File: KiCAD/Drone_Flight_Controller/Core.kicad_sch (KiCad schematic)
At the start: 24 parts, among them SW1 SW_Push, SW2 SW_Push, U5 BNO055, U6 ESP32-S3-MINI-1, U7 DPS368, U8 TLV75533PDBV

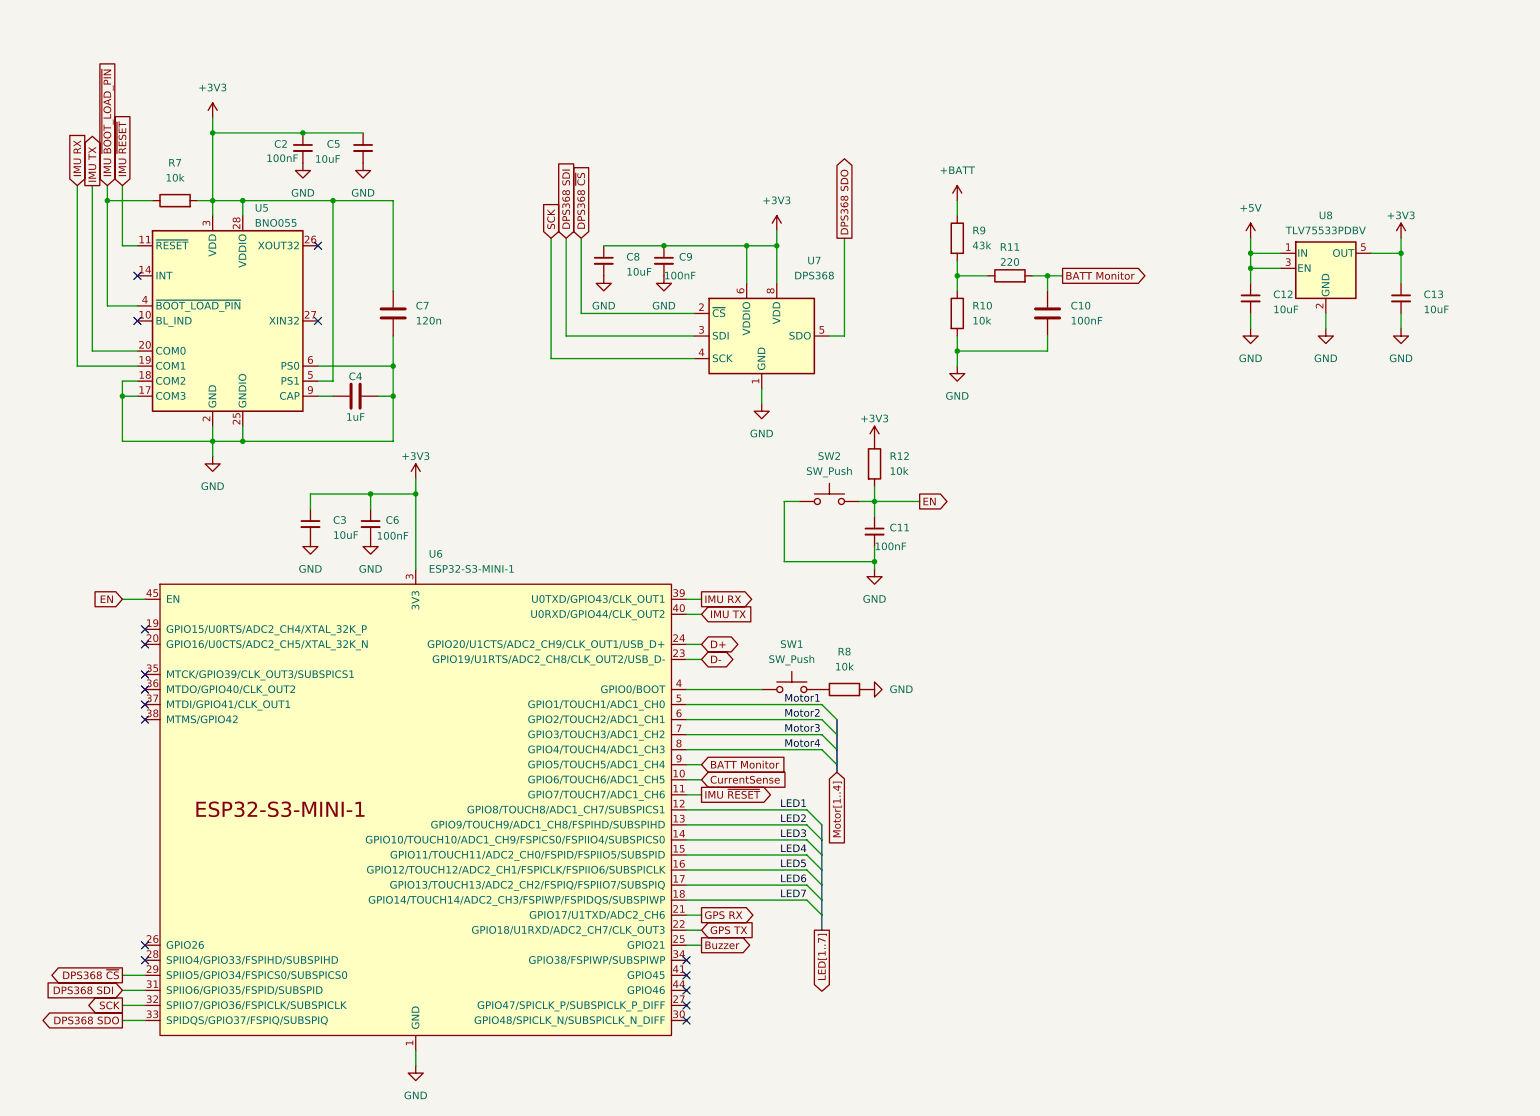
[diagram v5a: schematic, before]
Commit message: Add µSD Card Holder
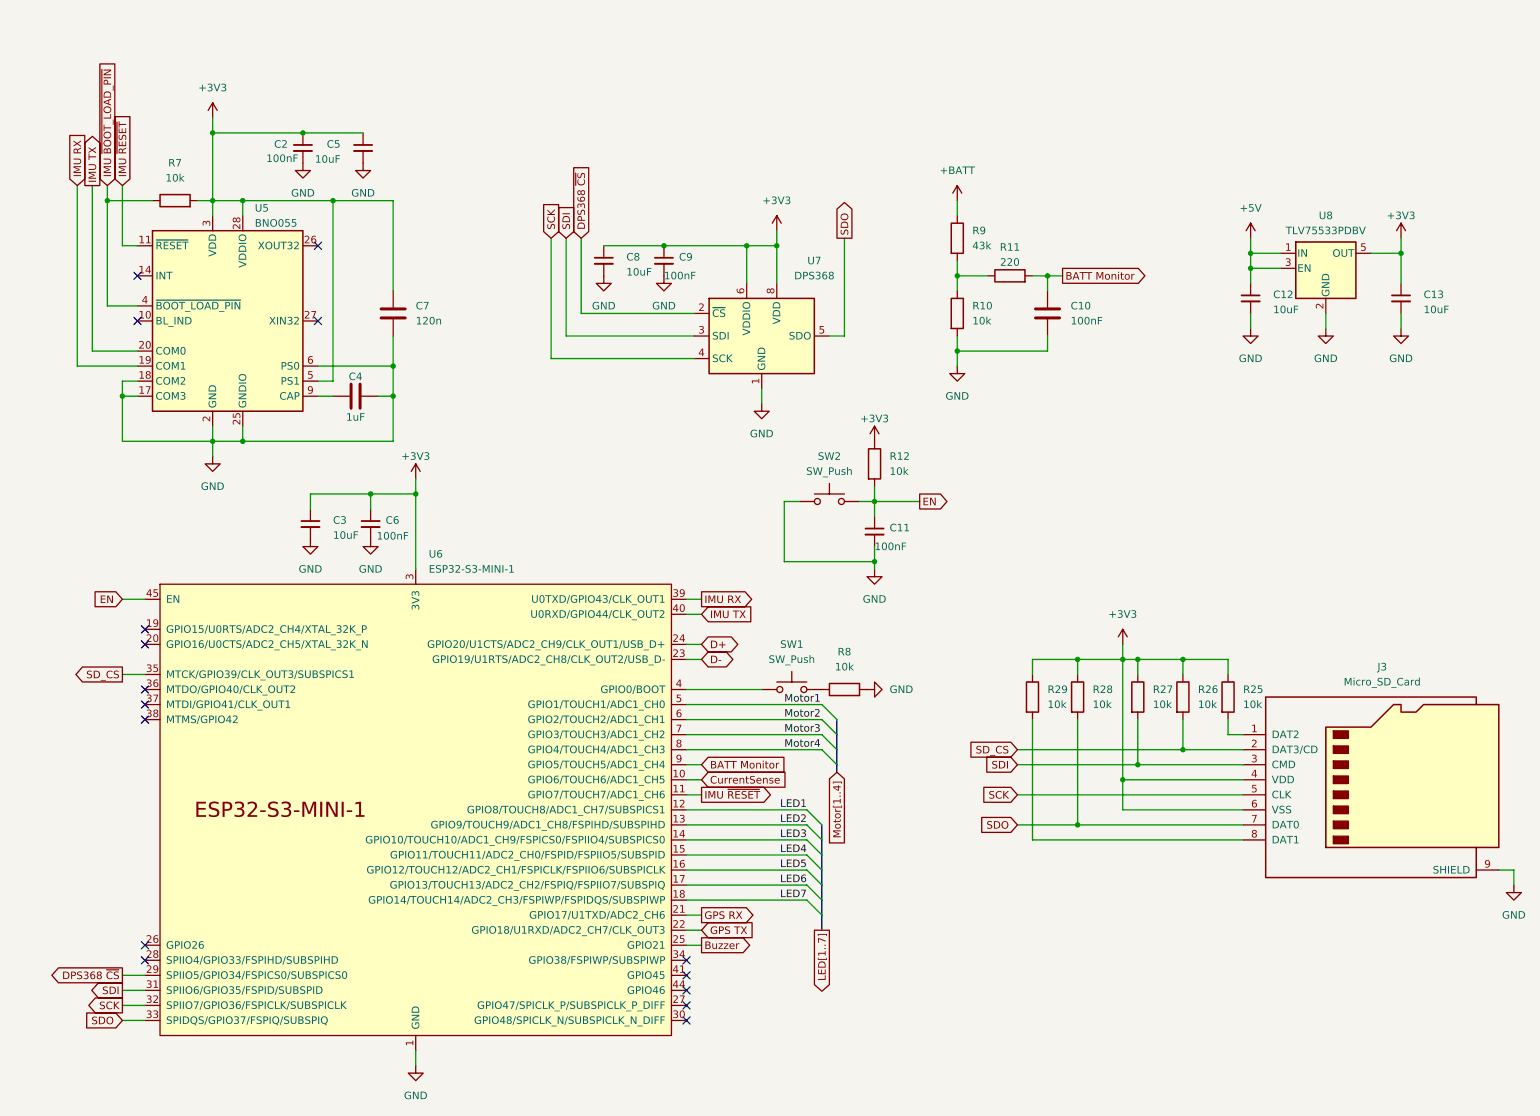
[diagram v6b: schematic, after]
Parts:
- added J3: Micro_SD_Card, Connector_Card:microSD_HC_Hirose_DM3D-SF, symbol Connector:Micro_SD_Card
- added R25, R26, R27, R28, R29: 10k, Resistor_SMD:R_0805_2012Metric_Pad1.20x1.40mm_HandSolder, symbol Device:R
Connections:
- net +3V3: now also J3.4 (VDD), J3.6 (VSS), R25.1, R26.1, R27.1, R28.1, R29.1
- net GND: now also J3.9 (SHIELD)
- net SCK: now also J3.5 (CLK)
- net SD_CS: now reaches U6.35 (MTCK/GPIO39/CLK_OUT3/SUBSPICS1)
- net SD_CS: now also J3.2 (DAT3/CD), R26.2
- net DPS368 SDI renamed SDI
- net SDI: now also J3.3 (CMD), R27.2
- net DPS368 SDO renamed SDO
- net SDO: now also J3.7 (DAT0), R28.2
- new net: J3.1 (DAT2), R25.2
- new net: J3.8 (DAT1), R29.2
- no-connect marks 17 -> 16

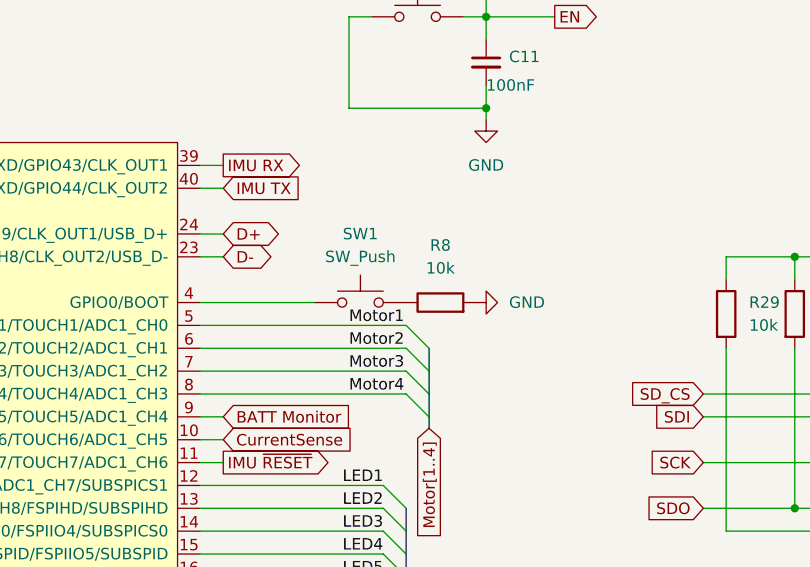
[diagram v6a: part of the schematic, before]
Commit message: Add debouncing C to button
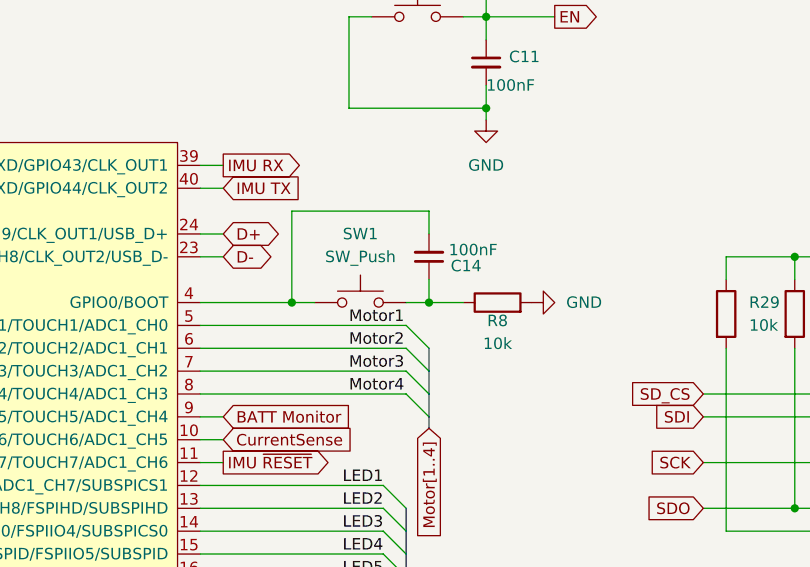
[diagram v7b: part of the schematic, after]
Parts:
- added C14: 100nF, Capacitor_SMD:C_0805_2012Metric, symbol Device:C_Small
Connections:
- net at SW1.1, U6.4 (GPIO0/BOOT): now also C14.2
- net at R8.1, SW1.2: now also C14.1
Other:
- moved on the sheet: R8
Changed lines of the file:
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@@
 	)
 	(junction
+		(at 158.75 123.19)
+		(diameter 0)
+		(color 0 0 0 0)
+	)
+	(junction
 		(at 209.55 135.89)
 		(diameter 0)
@@
 	)
 	(junction
+		(at 143.51 123.19)
+		(diameter 0)
+		(color 0 0 0 0)
+	)
+	(junction
 		(at 254 49.53)
 		(diameter 0)
@@
 	(wire
 		(pts
+			(xy 158.75 113.03) (xy 143.51 113.03)
+		)
+		(stroke
+			(width 0)
+			(type default)
+		)
+	)
+	(wire
+		(pts
 			(xy 87.63 87.63) (xy 87.63 90.17)
 		)
@@
 	(wire
 		(pts
+			(xy 143.51 113.03) (xy 143.51 123.19)
+		)
+		(stroke
+			(width 0)
+			(type default)
+		)
+	)
+	(wire
+		(pts
 			(xy 254 49.53) (xy 254 46.99)
 		)
@@
 	(wire
 		(pts
+			(xy 162.56 123.19) (xy 158.75 123.19)
+		)
+		(stroke
+			(width 0)
+			(type default)
+		)
+	)
+	(wire
+		(pts
 			(xy 50.8 40.64) (xy 53.34 40.64)
 		)
@@
 	(wire
 		(pts
+			(xy 158.75 120.65) (xy 158.75 123.19)
+		)
+		(stroke
+			(width 0)
+			(type default)
+		)
+	)
+	(wire
+		(pts
 			(xy 83.82 63.5) (xy 83.82 68.58)
 		)
@@
 	(wire
 		(pts
-			(xy 133.35 123.19) (xy 146.05 123.19)
+			(xy 133.35 123.19) (xy 143.51 123.19)
 		)
 		(stroke
@@
 	(wire
 		(pts
+			(xy 158.75 115.57) (xy 158.75 113.03)
+		)
+		(stroke
+			(width 0)
+			(type default)
+		)
+	)
+	(wire
+		(pts
 			(xy 179.07 68.58) (xy 179.07 66.04)
 		)
@@
 	(wire
 		(pts
+			(xy 143.51 123.19) (xy 146.05 123.19)
+		)
+		(stroke
+			(width 0)
+			(type default)
+		)
+	)
+	(wire
+		(pts
 			(xy 162.56 91.44) (xy 165.1 91.44)
 		)
@@
 	(wire
 		(pts
+			(xy 158.75 123.19) (xy 156.21 123.19)
+		)
+		(stroke
+			(width 0)
+			(type default)
+		)
+	)
+	(wire
+		(pts
 			(xy 115.57 59.69) (xy 134.62 59.69)
 		)
@@
 	(symbol
 		(lib_id "power:GND")
-		(at 163.83 123.19 90)
+		(at 170.18 123.19 90)
 		(unit 1)
 		(exclude_from_sim no)
@@
 		(fields_autoplaced yes)
 		(property "Reference" "#PWR049"
-			(at 170.18 123.19 0)
+			(at 176.53 123.19 0)
 			(effects
 				(font
@@
 		)
 		(property "Value" "GND"
-			(at 167.64 123.1899 90)
+			(at 173.99 123.1899 90)
 			(effects
 				(font
@@
 		)
 		(property "Footprint" ""
-			(at 163.83 123.19 0)
+			(at 170.18 123.19 0)
 			(effects
 				(font
@@
 		)
 		(property "Datasheet" ""
-			(at 163.83 123.19 0)
+			(at 170.18 123.19 0)
 			(effects
 				(font
@@
 		)
 		(property "Description" "Power symbol creates a global label with name \"GND\" , ground"
-			(at 163.83 123.19 0)
+			(at 170.18 123.19 0)
 			(effects
 				(font
@@
 	(symbol
 		(lib_id "Device:C_Small")
+		(at 158.75 118.11 180)
+		(unit 1)
+		(exclude_from_sim no)
+		(in_bom yes)
+		(on_board yes)
+		(dnp no)
+		(property "Reference" "C14"
+			(at 164.592 119.126 0)
+			(effects
+				(font
+					(size 1.27 1.27)
+				)
+				(justify left)
+			)
+		)
+		(property "Value" "100nF"
+			(at 166.37 117.348 0)
+			(effects
+				(font
+					(size 1.27 1.27)
+				)
+				(justify left)
+			)
+		)
+		(property "Footprint" "Capacitor_SMD:C_0805_2012Metric"
+			(at 158.75 118.11 0)
+			(effects
+				(font
+					(size 1.27 1.27)
+				)
+				(hide yes)
+			)
+		)
+		(property "Datasheet" "~"
+			(at 158.75 118.11 0)
+			(effects
+				(font
+					(size 1.27 1.27)
+				)
+				(hide yes)
+			)
+		)
+		(property "Description" "Unpolarized capacitor, small symbol"
+			(at 158.75 118.11 0)
+			(effects
+				(font
+					(size 1.27 1.27)
+				)
+				(hide yes)
+			)
+		)
+		(pin "1"
+		)
+		(pin "2"
+		)
+		(instances
+			(project "Drone_Flight_Controller"
+				(path "/51ab9491-7068-4b24-bb38-47a0c739796e/c31581c9-6b89-48da-8db2-6196211c3da7"
+					(reference "C14")
+					(unit 1)
+				)
+			)
+		)
+	)
+	(symbol
+		(lib_id "Device:C_Small")
 		(at 80.01 95.25 0)
 		(unit 1)
@@
 	(symbol
 		(lib_id "Device:R")
-		(at 160.02 123.19 90)
+		(at 166.37 123.19 90)
 		(unit 1)
 		(exclude_from_sim no)
@@
 		(on_board yes)
 		(dnp no)
-		(fields_autoplaced yes)
 		(property "Reference" "R8"
-			(at 160.02 116.84 90)
+			(at 166.37 125.222 90)
 			(effects
 				(font
@@
 		)
 		(property "Value" "10k"
-			(at 160.02 119.38 90)
+			(at 166.37 127.762 90)
 			(effects
 				(font
@@
 		)
 		(property "Footprint" "Resistor_SMD:R_0805_2012Metric_Pad1.20x1.40mm_HandSolder"
-			(at 160.02 124.968 90)
+			(at 166.37 124.968 90)
 			(effects
 				(font
@@
 		)
 		(property "Datasheet" "~"
-			(at 160.02 123.19 0)
+			(at 166.37 123.19 0)
 			(effects
 				(font
@@
 		)
 		(property "Description" "Resistor"
-			(at 160.02 123.19 0)
+			(at 166.37 123.19 0)
 			(effects
 				(font

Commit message: routing
routing
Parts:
- J3: footprint Connector_Card:microSD_HC_Hirose_DM3D-SF -> uSD_Card:502570-0893_MOL
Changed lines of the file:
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@@
 			)
 		)
-		(property "Footprint" "Connector_Card:microSD_HC_Hirose_DM3D-SF"
+		(property "Footprint" "uSD_Card:502570-0893_MOL"
 			(at 279.4 130.81 0)
 			(effects
@@
 			)
 		)
-		(property "Datasheet" "https://www.we-online.com/components/products/datasheet/693072010801.pdf"
+		(property "Datasheet" "https://www.molex.com/en-us/products/part-detail-pdf/5025700893?display=pdf"
 			(at 250.19 138.43 0)
 			(effects
